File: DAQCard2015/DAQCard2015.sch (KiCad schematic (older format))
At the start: 0 parts

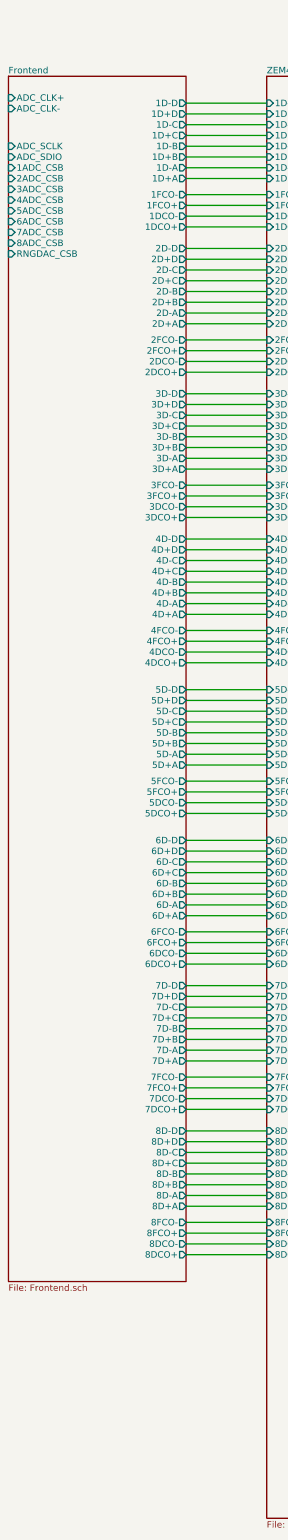
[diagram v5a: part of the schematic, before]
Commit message: Updates to DAQ Board focusing on the power system and flood fills for it
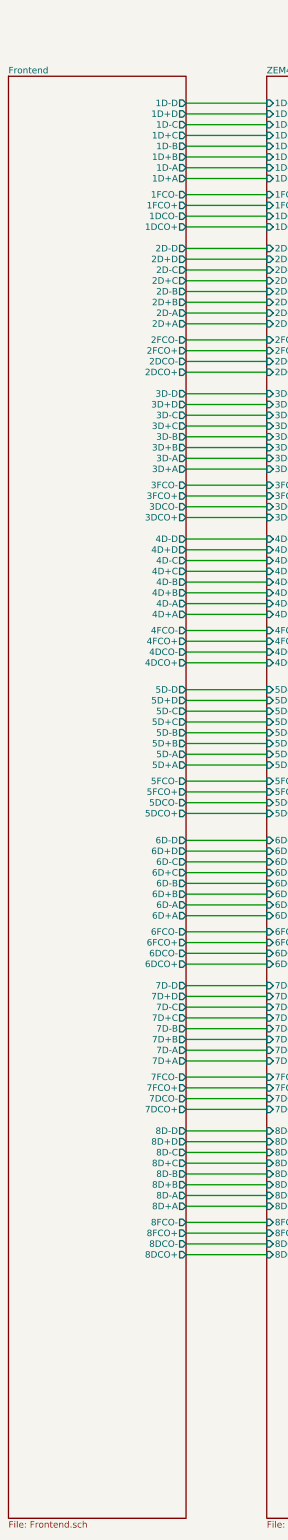
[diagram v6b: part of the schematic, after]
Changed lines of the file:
@@
 $EndDescr
-$Sheet
-S 2150 2250 1650 11200
-U 55C47A4C
-F0 "Frontend" 60
-F1 "Frontend.sch" 60
-F2 "ADC_CLK+" I L 2150 2450 60
-F3 "ADC_CLK-" I L 2150 2550 60
-F4 "1D-D" O R 3800 2500 60
-F5 "1D+D" O R 3800 2600 60
-F6 "1D-C" O R 3800 2700 60
-F7 "1D+C" O R 3800 2800 60
-F8 "1D-B" O R 3800 2900 60
-F9 "1D+B" O R 3800 3000 60
-F10 "1D-A" O R 3800 3100 60
-F11 "1D+A" O R 3800 3200 60
-F12 "1FCO-" O R 3800 3350 60
-F13 "1FCO+" O R 3800 3450 60
-F14 "1DCO-" O R 3800 3550 60
-F15 "1DCO+" O R 3800 3650 60
-F16 "2D-D" O R 3800 3850 60
-F17 "2D+D" O R 3800 3950 60
-F18 "2D-C" O R 3800 4050 60
-F19 "2D+C" O R 3800 4150 60
-F20 "2D-B" O R 3800 4250 60
-F21 "2D+B" O R 3800 4350 60
-F22 "2D-A" O R 3800 4450 60
-F23 "2D+A" O R 3800 4550 60
-F24 "2FCO-" O R 3800 4700 60
-F25 "2FCO+" O R 3800 4800 60
-F26 "2DCO-" O R 3800 4900 60
-F27 "2DCO+" O R 3800 5000 60
-F28 "4D+D" O R 3800 6650 60
-F29 "4D-C" O R 3800 6750 60
-F30 "4D+C" O R 3800 6850 60
-F31 "4D-B" O R 3800 6950 60
-F32 "4D+B" O R 3800 7050 60
-F33 "4D-A" O R 3800 7150 60
-F34 "4D+A" O R 3800 7250 60
-F35 "4FCO-" O R 3800 7400 60
-F36 "4FCO+" O R 3800 7500 60
-F37 "4DCO-" O R 3800 7600 60
-F38 "4DCO+" O R 3800 7700 60
-F39 "3D-D" O R 3800 5200 60
-F40 "3D+D" O R 3800 5300 60
-F41 "3D-C" O R 3800 5400 60
-F42 "3D+C" O R 3800 5500 60
-F43 "3D-B" O R 3800 5600 60
-F44 "3D+B" O R 3800 5700 60
-F45 "3D-A" O R 3800 5800 60
-F46 "3D+A" O R 3800 5900 60
-F47 "3FCO-" O R 3800 6050 60
-F48 "3FCO+" O R 3800 6150 60
-F49 "3DCO-" O R 3800 6250 60
-F50 "3DCO+" O R 3800 6350 60
-F51 "ADC_SCLK" I L 2150 2900 60
-F52 "ADC_SDIO" I L 2150 3000 60
-F53 "1ADC_CSB" I L 2150 3100 60
-F54 "8D-D" O R 3800 12050 60
-F55 "8D+D" O R 3800 12150 60
-F56 "8D-C" O R 3800 12250 60
-F57 "8D+C" O R 3800 12350 60
-F58 "8D-B" O R 3800 12450 60
-F59 "8D+B" O R 3800 12550 60
-F60 "8D-A" O R 3800 12650 60
-F61 "8D+A" O R 3800 12750 60
-F62 "8FCO-" O R 3800 12900 60
-F63 "8FCO+" O R 3800 13000 60
-F64 "8DCO-" O R 3800 13100 60
-F65 "8DCO+" O R 3800 13200 60
-F66 "7D-D" O R 3800 10700 60
-F67 "7D+D" O R 3800 10800 60
-F68 "7D-C" O R 3800 10900 60
-F69 "7D+C" O R 3800 11000 60
-F70 "7D-B" O R 3800 11100 60
-F71 "7D+B" O R 3800 11200 60
-F72 "7D-A" O R 3800 11300 60
-F73 "7D+A" O R 3800 11400 60
-F74 "7FCO-" O R 3800 11550 60
-F75 "7FCO+" O R 3800 11650 60
-F76 "7DCO-" O R 3800 11750 60
-F77 "7DCO+" O R 3800 11850 60
-F78 "5D-D" O R 3800 7950 60
-F79 "5D+D" O R 3800 8050 60
-F80 "5D-C" O R 3800 8150 60
-F81 "5D+C" O R 3800 8250 60
-F82 "5D-B" O R 3800 8350 60
-F83 "5D+B" O R 3800 8450 60
-F84 "5D-A" O R 3800 8550 60
-F85 "5D+A" O R 3800 8650 60
-F86 "5FCO-" O R 3800 8800 60
-F87 "5FCO+" O R 3800 8900 60
-F88 "5DCO-" O R 3800 9000 60
-F89 "5DCO+" O R 3800 9100 60
-F90 "6D-D" O R 3800 9350 60
-F91 "6D+D" O R 3800 9450 60
-F92 "6D-C" O R 3800 9550 60
-F93 "6D+C" O R 3800 9650 60
-F94 "6D-B" O R 3800 9750 60
-F95 "6D+B" O R 3800 9850 60
-F96 "6D-A" O R 3800 9950 60
-F97 "6D+A" O R 3800 10050 60
-F98 "6FCO-" O R 3800 10200 60
-F99 "6FCO+" O R 3800 10300 60
-F100 "6DCO-" O R 3800 10400 60
-F101 "6DCO+" O R 3800 10500 60
-F102 "4D-D" O R 3800 6550 60
-F103 "2ADC_CSB" I L 2150 3200 60
-F104 "3ADC_CSB" I L 2150 3300 60
-F105 "4ADC_CSB" I L 2150 3400 60
-F106 "5ADC_CSB" I L 2150 3500 60
-F107 "6ADC_CSB" I L 2150 3600 60
-F108 "7ADC_CSB" I L 2150 3700 60
-F109 "8ADC_CSB" I L 2150 3800 60
-F110 "RNGDAC_CSB" I L 2150 3900 60
-$EndSheet
 $Sheet
 S 4550 2250 3150 13400
@@
 Wire Wire Line
 	3800 13200 4550 13200
+$Sheet
+S 2150 2250 1650 13400
+U 55C47A4C
+F0 "Frontend" 60
+F1 "Frontend.sch" 60
+F2 "1D-D" O R 3800 2500 60
+F3 "1D+D" O R 3800 2600 60
+F4 "1D-C" O R 3800 2700 60
+F5 "1D+C" O R 3800 2800 60
+F6 "1D-B" O R 3800 2900 60
+F7 "1D+B" O R 3800 3000 60
+F8 "1D-A" O R 3800 3100 60
+F9 "1D+A" O R 3800 3200 60
+F10 "1FCO-" O R 3800 3350 60
+F11 "1FCO+" O R 3800 3450 60
+F12 "1DCO-" O R 3800 3550 60
+F13 "1DCO+" O R 3800 3650 60
+F14 "2D-D" O R 3800 3850 60
+F15 "2D+D" O R 3800 3950 60
+F16 "2D-C" O R 3800 4050 60
+F17 "2D+C" O R 3800 4150 60
+F18 "2D-B" O R 3800 4250 60
+F19 "2D+B" O R 3800 4350 60
+F20 "2D-A" O R 3800 4450 60
+F21 "2D+A" O R 3800 4550 60
+F22 "2FCO-" O R 3800 4700 60
+F23 "2FCO+" O R 3800 4800 60
+F24 "2DCO-" O R 3800 4900 60
+F25 "2DCO+" O R 3800 5000 60
+F26 "4D+D" O R 3800 6650 60
+F27 "4D-C" O R 3800 6750 60
+F28 "4D+C" O R 3800 6850 60
+F29 "4D-B" O R 3800 6950 60
+F30 "4D+B" O R 3800 7050 60
+F31 "4D-A" O R 3800 7150 60
+F32 "4D+A" O R 3800 7250 60
+F33 "4FCO-" O R 3800 7400 60
+F34 "4FCO+" O R 3800 7500 60
+F35 "4DCO-" O R 3800 7600 60
+F36 "4DCO+" O R 3800 7700 60
+F37 "3D-D" O R 3800 5200 60
+F38 "3D+D" O R 3800 5300 60
+F39 "3D-C" O R 3800 5400 60
+F40 "3D+C" O R 3800 5500 60
+F41 "3D-B" O R 3800 5600 60
+F42 "3D+B" O R 3800 5700 60
+F43 "3D-A" O R 3800 5800 60
+F44 "3D+A" O R 3800 5900 60
+F45 "3FCO-" O R 3800 6050 60
+F46 "3FCO+" O R 3800 6150 60
+F47 "3DCO-" O R 3800 6250 60
+F48 "3DCO+" O R 3800 6350 60
+F49 "8D-D" O R 3800 12050 60
+F50 "8D+D" O R 3800 12150 60
+F51 "8D-C" O R 3800 12250 60
+F52 "8D+C" O R 3800 12350 60
+F53 "8D-B" O R 3800 12450 60
+F54 "8D+B" O R 3800 12550 60
+F55 "8D-A" O R 3800 12650 60
+F56 "8D+A" O R 3800 12750 60
+F57 "8FCO-" O R 3800 12900 60
+F58 "8FCO+" O R 3800 13000 60
+F59 "8DCO-" O R 3800 13100 60
+F60 "8DCO+" O R 3800 13200 60
+F61 "7D-D" O R 3800 10700 60
+F62 "7D+D" O R 3800 10800 60
+F63 "7D-C" O R 3800 10900 60
+F64 "7D+C" O R 3800 11000 60
+F65 "7D-B" O R 3800 11100 60
+F66 "7D+B" O R 3800 11200 60
+F67 "7D-A" O R 3800 11300 60
+F68 "7D+A" O R 3800 11400 60
+F69 "7FCO-" O R 3800 11550 60
+F70 "7FCO+" O R 3800 11650 60
+F71 "7DCO-" O R 3800 11750 60
+F72 "7DCO+" O R 3800 11850 60
+F73 "5D-D" O R 3800 7950 60
+F74 "5D+D" O R 3800 8050 60
+F75 "5D-C" O R 3800 8150 60
+F76 "5D+C" O R 3800 8250 60
+F77 "5D-B" O R 3800 8350 60
+F78 "5D+B" O R 3800 8450 60
+F79 "5D-A" O R 3800 8550 60
+F80 "5D+A" O R 3800 8650 60
+F81 "5FCO-" O R 3800 8800 60
+F82 "5FCO+" O R 3800 8900 60
+F83 "5DCO-" O R 3800 9000 60
+F84 "5DCO+" O R 3800 9100 60
+F85 "6D-D" O R 3800 9350 60
+F86 "6D+D" O R 3800 9450 60
+F87 "6D-C" O R 3800 9550 60
+F88 "6D+C" O R 3800 9650 60
+F89 "6D-B" O R 3800 9750 60
+F90 "6D+B" O R 3800 9850 60
+F91 "6D-A" O R 3800 9950 60
+F92 "6D+A" O R 3800 10050 60
+F93 "6FCO-" O R 3800 10200 60
+F94 "6FCO+" O R 3800 10300 60
+F95 "6DCO-" O R 3800 10400 60
+F96 "6DCO+" O R 3800 10500 60
+F97 "4D-D" O R 3800 6550 60
+$EndSheet
 $EndSCHEMATC

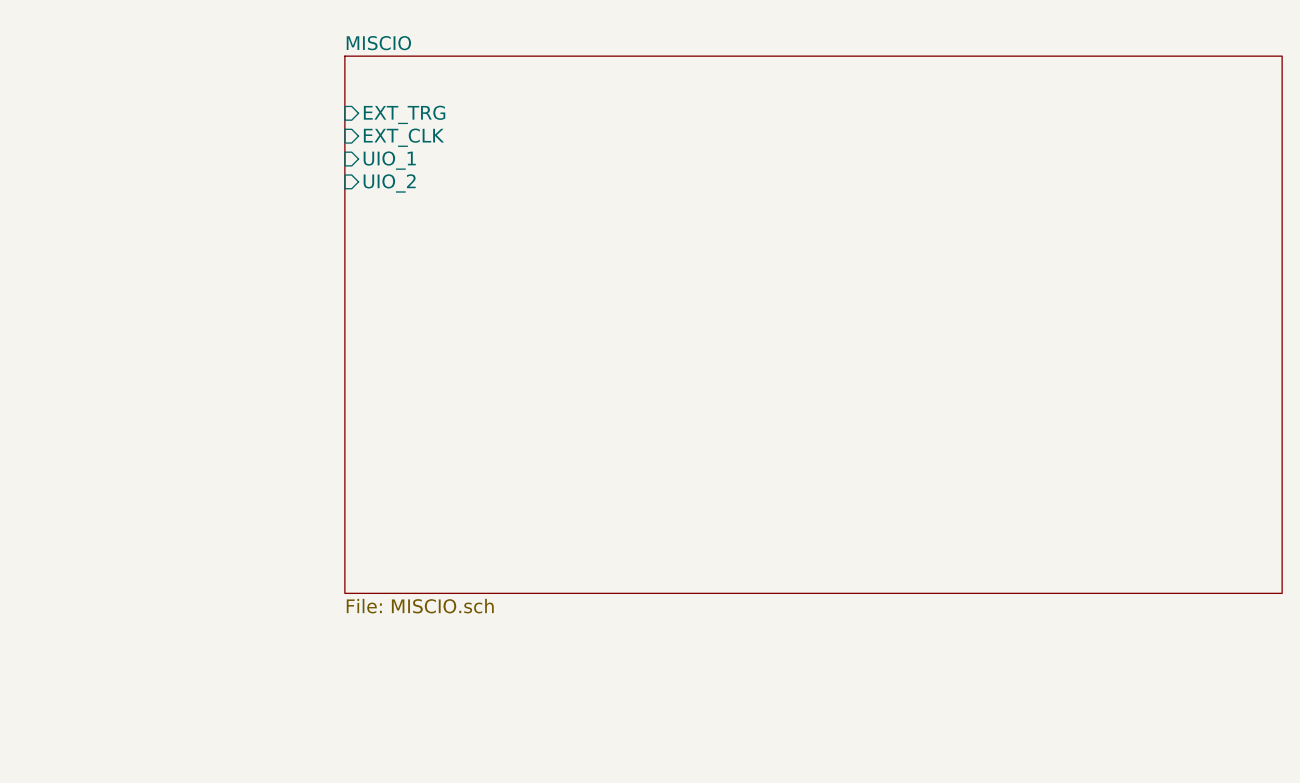
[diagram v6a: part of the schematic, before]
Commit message: Adds APC128 connections and voltage supplies
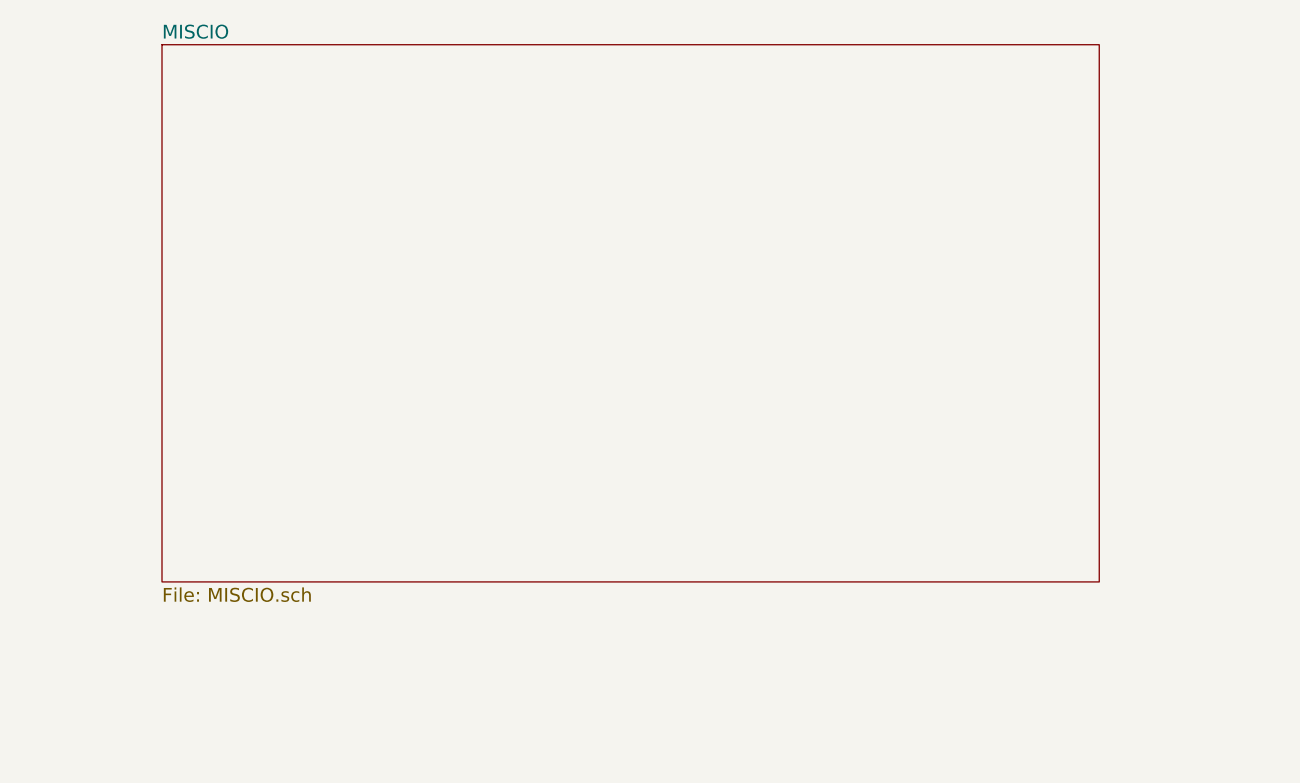
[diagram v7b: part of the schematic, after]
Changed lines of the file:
@@
 $EndSheet
 $Sheet
-S 18200 1700 4100 2350
+S 17400 1650 4100 2350
 U 55C9D43F
 F0 "MISCIO" 60
 F1 "MISCIO.sch" 60
-F2 "EXT_TRG" I L 18200 1950 60
-F3 "EXT_CLK" I L 18200 2050 60
-F4 "UIO_1" I L 18200 2150 60
-F5 "UIO_2" I L 18200 2250 60
 $EndSheet
 $Sheet

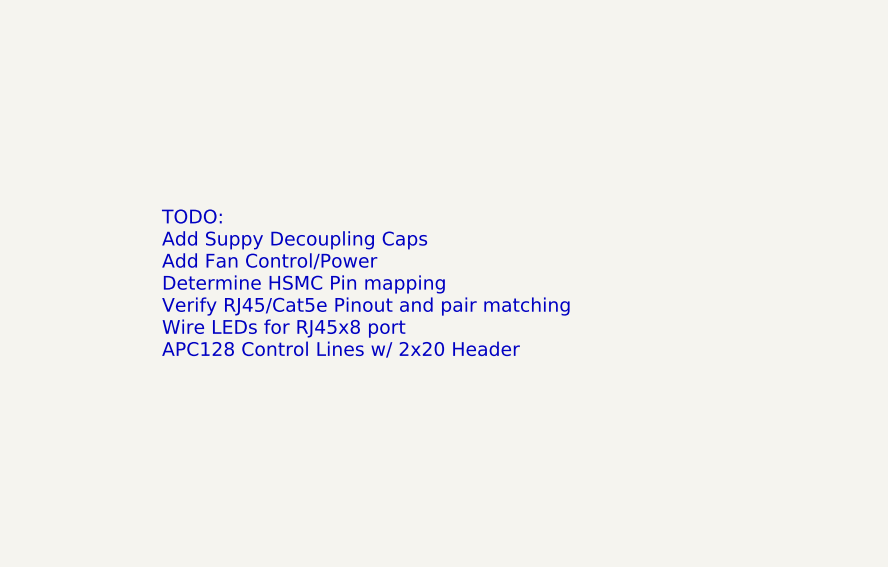
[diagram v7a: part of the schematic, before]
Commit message: Update to DAQ Board including adding an JTAG header and hooking up external clock and trigger
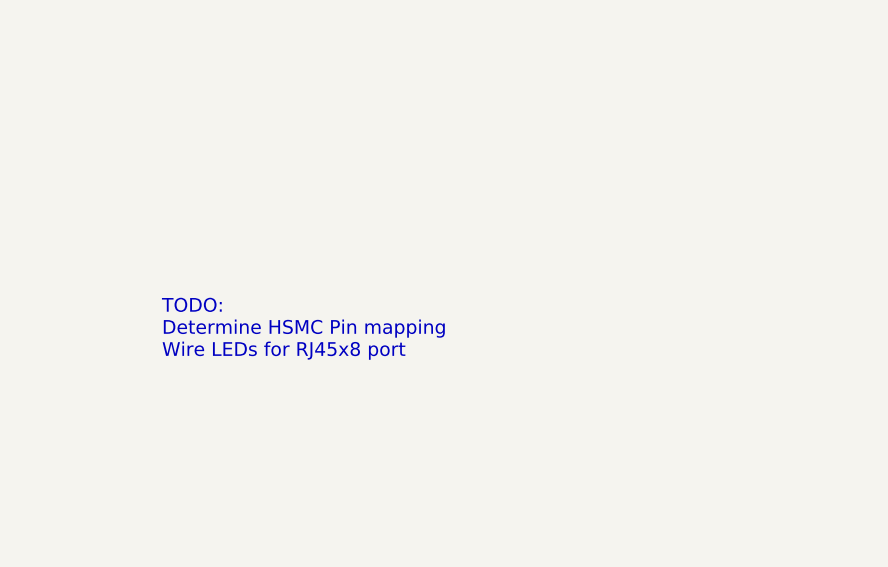
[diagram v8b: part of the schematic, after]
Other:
- note added: "TODO:\nDetermine HSMC Pin mapping\nWire LEDs for RJ45x8 port"
- note removed: "TODO:\nAdd Suppy Decoupling Caps\nAdd Fan Control/Power\nDetermine HSMC Pin mapping\nVerify RJ45/Cat5e Pinout and pair matching\nWire LEDs for RJ45x8 port\nAPC128 Control Lines w/ 2x20 Header"
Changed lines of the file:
@@
 	3800 3650 4550 3650
 Text Notes 14100 9250 0    60   ~ 0
-TODO:\nAdd Suppy Decoupling Caps\nAdd Fan Control/Power\nDetermine HSMC Pin mapping\nVerify RJ45/Cat5e Pinout and pair matching\nWire LEDs for RJ45x8 port\nAPC128 Control Lines w/ 2x20 Header
+TODO:\nDetermine HSMC Pin mapping\nWire LEDs for RJ45x8 port
 Wire Wire Line
 	3800 3850 4550 3850
